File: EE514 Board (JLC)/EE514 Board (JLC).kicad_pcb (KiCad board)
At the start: 4 copper layers, 92.2 x 66.5 mm, 52 parts, among them J101 Screw_Terminal_01x02, J102 SMA, J103 SMA, J104 SMA, J105 SMA, J106 SMA, Q301 BFP620, Q501 BFP620, U201 TLC2201, U401 TLC2201

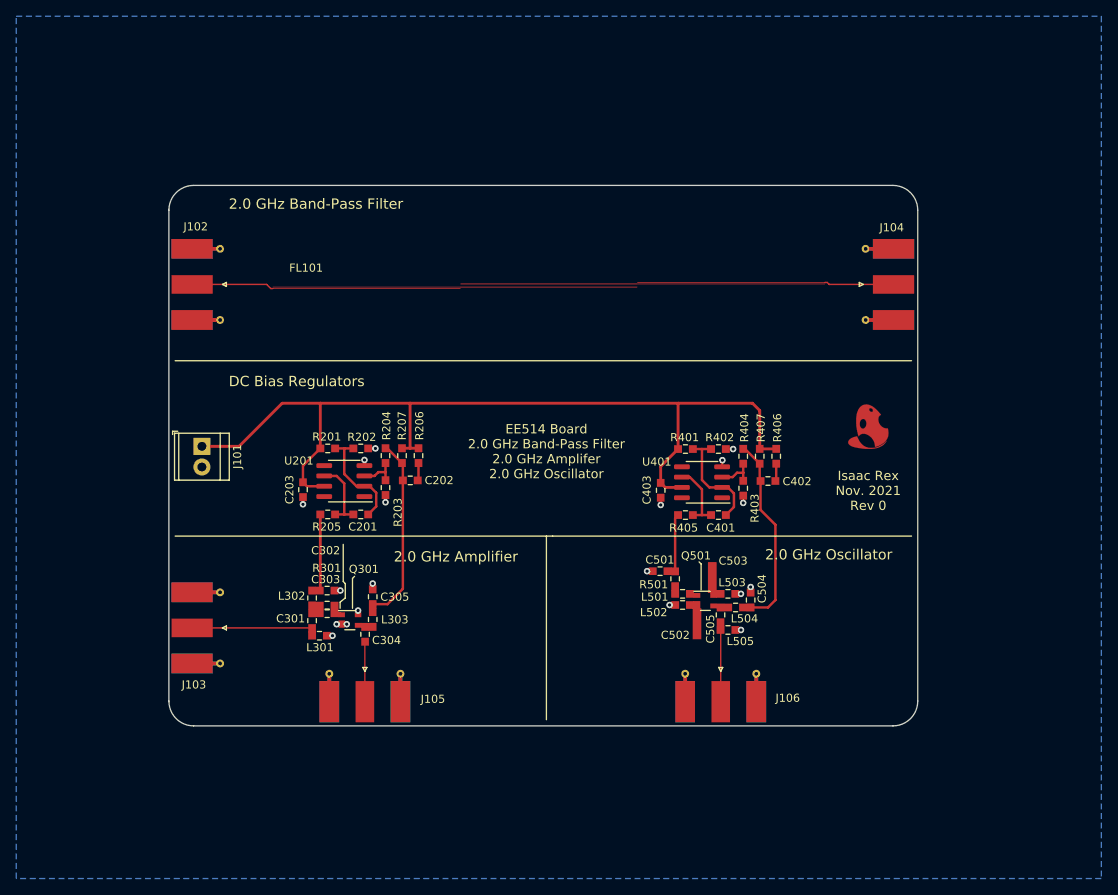
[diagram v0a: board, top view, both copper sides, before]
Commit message: Updated JLC board with edge fence and edge soldermask pullback
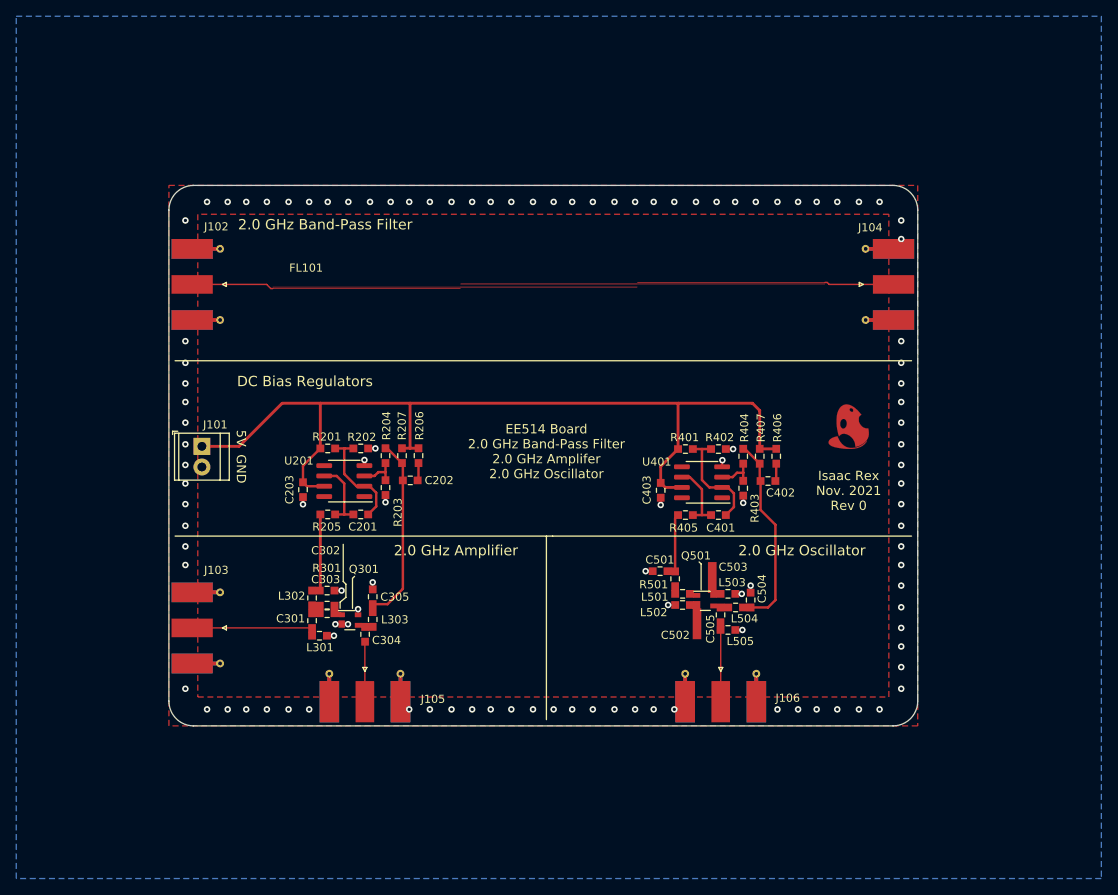
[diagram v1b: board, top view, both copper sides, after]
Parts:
- moved G*** 2.41 mm to (190.4, 97.3)
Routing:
- net GND: vias 19 -> 113
- added copper zone on F.Cu, net GND
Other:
- board text added: "5V"
- board text added: "GND"
